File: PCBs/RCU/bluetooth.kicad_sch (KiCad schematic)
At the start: 33 parts

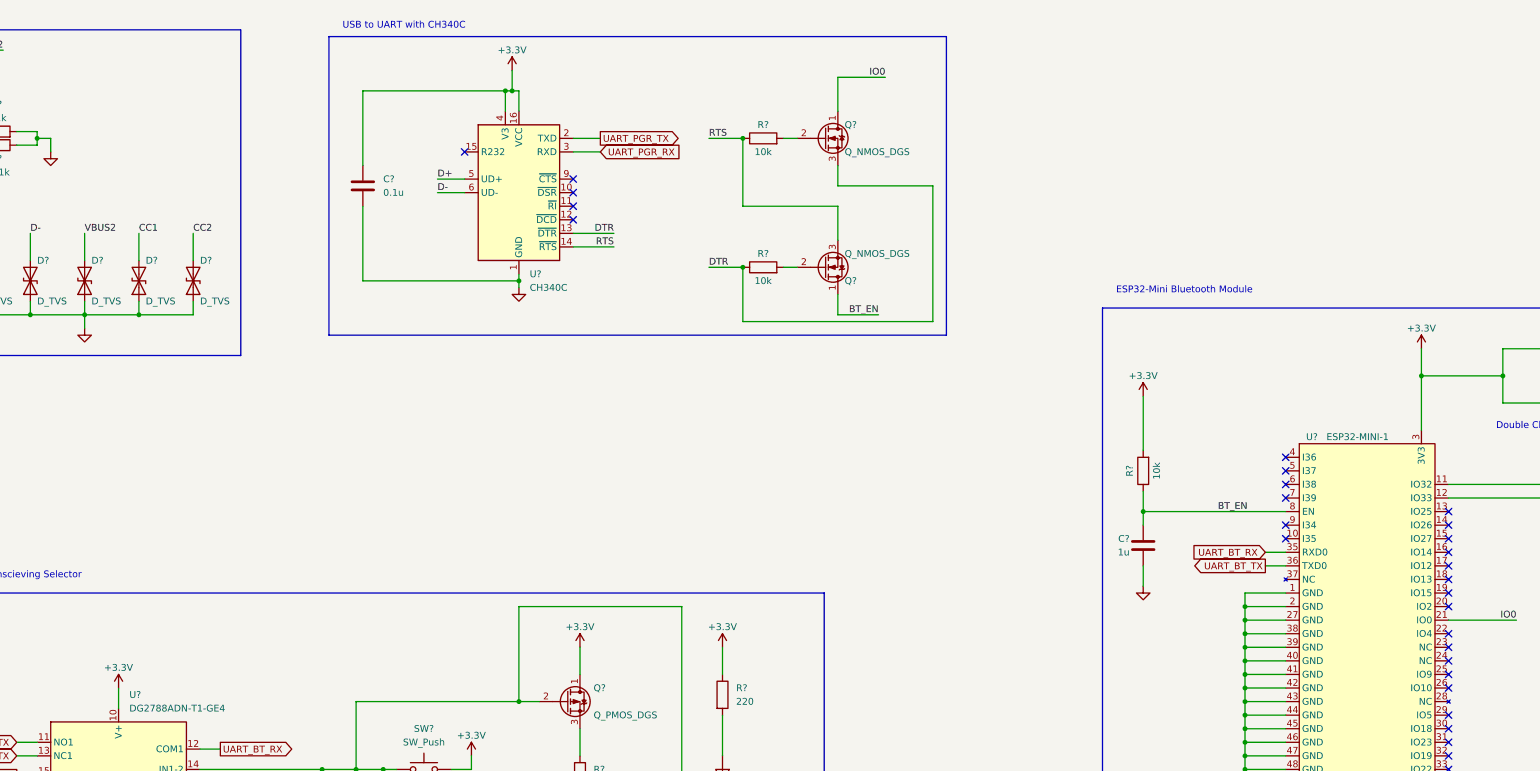
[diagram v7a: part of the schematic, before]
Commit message: Add battery filter circuit, corrected cap values for 3.3V regulators, used different output power floag for Bottom regulator so that it only powers the Bluetooth susbsystem
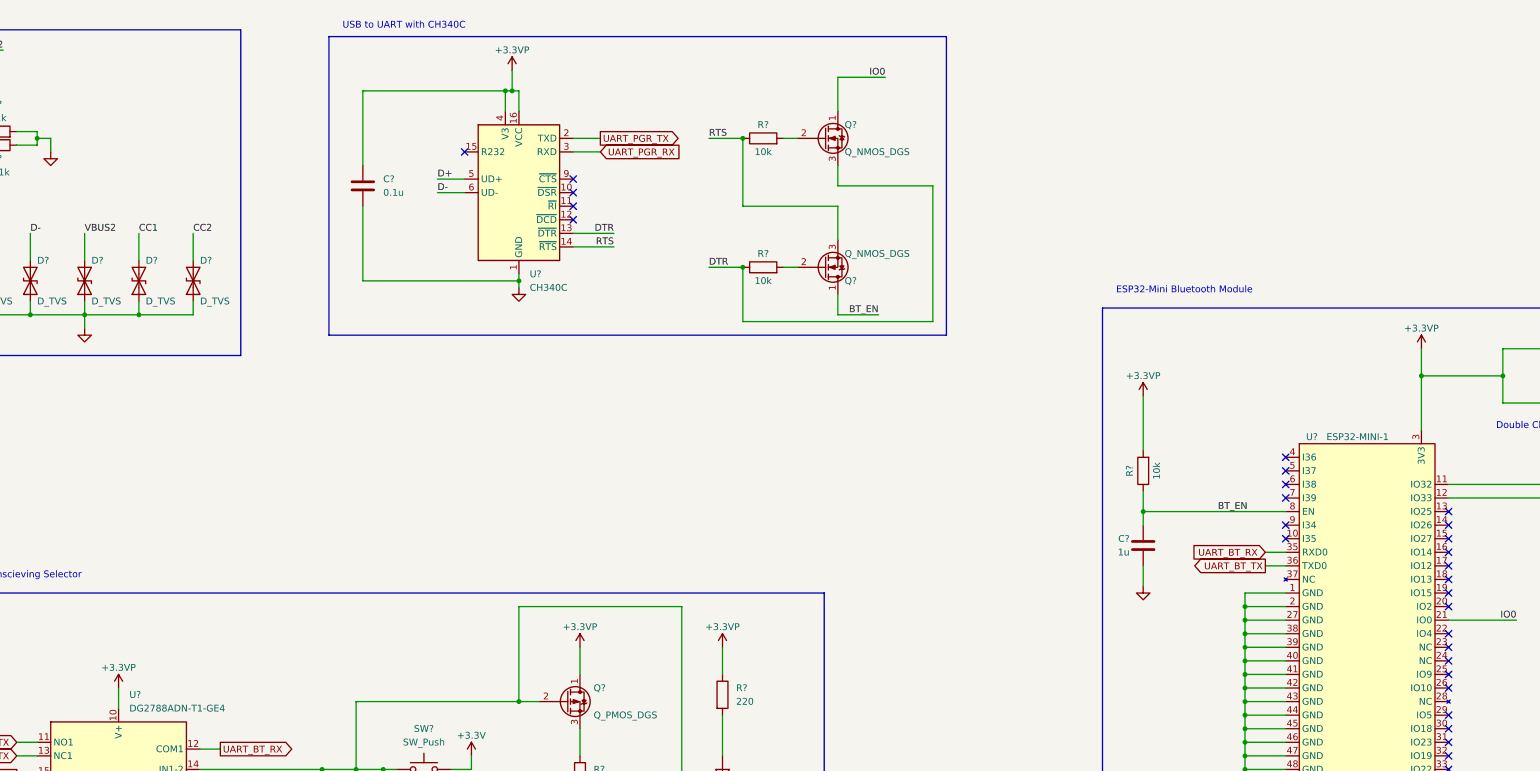
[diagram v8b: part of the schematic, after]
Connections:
- net +3V3: no longer C?.1, C?.1, C?.1, Q?.1 (D), R?.1, R?.2, U?.10 (V+), U?.16 (VCC), U?.3 (3V3), U?.4 (V3)
- new net +3.3VP: C?.1, C?.1, C?.1, Q?.1 (D), R?.1, R?.2, U?.10 (V+), U?.16 (VCC), U?.3 (3V3), U?.4 (V3)
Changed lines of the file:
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@@
     )
-  )
-  (symbol (lib_id "power:+3.3V") (at 340.36 91.44 0) (unit 1)
-    (in_bom yes) (on_board yes)
-    (property "Reference" "#PWR?" (id 0) (at 340.36 95.25 0)
-      (effects (font (size 1.27 1.27)) hide)
-    )
-    (property "Value" "+3.3V" (id 1) (at 340.36 87.63 0))
-    (property "Footprint" "" (id 2) (at 340.36 91.44 0)
-      (effects (font (size 1.27 1.27)) hide)
-    )
-    (property "Datasheet" "" (id 3) (at 340.36 91.44 0)
-      (effects (font (size 1.27 1.27)) hide)
-    )
-    (pin "1")
   )
   (symbol (lib_id "Device:C") (at 142.24 60.96 0) (unit 1)
@@
     (pin "1")
     (pin "2")
+  )
+  (symbol (lib_id "power:+3.3VP") (at 170.18 39.37 0) (unit 1)
+    (in_bom yes) (on_board yes)
+    (property "Reference" "#PWR?" (id 0) (at 173.99 40.64 0)
+      (effects (font (size 1.27 1.27)) hide)
+    )
+    (property "Value" "+3.3VP" (id 1) (at 170.18 35.56 0))
+    (property "Footprint" "" (id 2) (at 170.18 39.37 0)
+      (effects (font (size 1.27 1.27)) hide)
+    )
+    (property "Datasheet" "" (id 3) (at 170.18 39.37 0)
+      (effects (font (size 1.27 1.27)) hide)
+    )
+    (pin "1")
   )
   (symbol (lib_id "Device:Q_NMOS_DGS") (at 228.6 76.2 0) (mirror x) (unit 1)
@@
     )
     (property "Datasheet" "" (id 3) (at 288.29 135.89 0)
+      (effects (font (size 1.27 1.27)) hide)
+    )
+    (pin "1")
+  )
+  (symbol (lib_id "power:+3.3VP") (at 209.55 147.32 0) (unit 1)
+    (in_bom yes) (on_board yes)
+    (property "Reference" "#PWR?" (id 0) (at 213.36 148.59 0)
+      (effects (font (size 1.27 1.27)) hide)
+    )
+    (property "Value" "+3.3VP" (id 1) (at 209.55 143.51 0))
+    (property "Footprint" "" (id 2) (at 209.55 147.32 0)
+      (effects (font (size 1.27 1.27)) hide)
+    )
+    (property "Datasheet" "" (id 3) (at 209.55 147.32 0)
       (effects (font (size 1.27 1.27)) hide)
     )
@@
     (pin "2")
   )
-  (symbol (lib_id "power:+3.3V") (at 170.18 39.37 0) (unit 1)
-    (in_bom yes) (on_board yes)
-    (property "Reference" "#PWR?" (id 0) (at 170.18 43.18 0)
-      (effects (font (size 1.27 1.27)) hide)
-    )
-    (property "Value" "+3.3V" (id 1) (at 170.18 35.56 0))
-    (property "Footprint" "" (id 2) (at 170.18 39.37 0)
-      (effects (font (size 1.27 1.27)) hide)
-    )
-    (property "Datasheet" "" (id 3) (at 170.18 39.37 0)
+  (symbol (lib_id "power:+3.3VP") (at 340.36 91.44 0) (unit 1)
+    (in_bom yes) (on_board yes)
+    (property "Reference" "#PWR?" (id 0) (at 344.17 92.71 0)
+      (effects (font (size 1.27 1.27)) hide)
+    )
+    (property "Value" "+3.3VP" (id 1) (at 340.36 87.63 0))
+    (property "Footprint" "" (id 2) (at 340.36 91.44 0)
+      (effects (font (size 1.27 1.27)) hide)
+    )
+    (property "Datasheet" "" (id 3) (at 340.36 91.44 0)
+      (effects (font (size 1.27 1.27)) hide)
+    )
+    (pin "1")
+  )
+  (symbol (lib_id "power:+3.3VP") (at 182.88 147.32 0) (unit 1)
+    (in_bom yes) (on_board yes)
+    (property "Reference" "#PWR?" (id 0) (at 186.69 148.59 0)
+      (effects (font (size 1.27 1.27)) hide)
+    )
+    (property "Value" "+3.3VP" (id 1) (at 182.88 143.51 0))
+    (property "Footprint" "" (id 2) (at 182.88 147.32 0)
+      (effects (font (size 1.27 1.27)) hide)
+    )
+    (property "Datasheet" "" (id 3) (at 182.88 147.32 0)
       (effects (font (size 1.27 1.27)) hide)
     )
@@
     (pin "2")
   )
-  (symbol (lib_id "power:+3.3V") (at 182.88 147.32 0) (unit 1)
-    (in_bom yes) (on_board yes)
-    (property "Reference" "#PWR?" (id 0) (at 182.88 151.13 0)
-      (effects (font (size 1.27 1.27)) hide)
-    )
-    (property "Value" "+3.3V" (id 1) (at 182.88 143.51 0))
-    (property "Footprint" "" (id 2) (at 182.88 147.32 0)
-      (effects (font (size 1.27 1.27)) hide)
-    )
-    (property "Datasheet" "" (id 3) (at 182.88 147.32 0)
-      (effects (font (size 1.27 1.27)) hide)
-    )
-    (pin "1")
-  )
   (symbol (lib_id "Device:R") (at 209.55 156.21 0) (unit 1)
     (in_bom yes) (on_board yes) (fields_autoplaced)
@@
     (pin "1")
     (pin "2")
-  )
-  (symbol (lib_id "power:+3.3V") (at 96.52 154.94 0) (unit 1)
-    (in_bom yes) (on_board yes)
-    (property "Reference" "#PWR?" (id 0) (at 96.52 158.75 0)
-      (effects (font (size 1.27 1.27)) hide)
-    )
-    (property "Value" "+3.3V" (id 1) (at 96.52 151.13 0))
-    (property "Footprint" "" (id 2) (at 96.52 154.94 0)
-      (effects (font (size 1.27 1.27)) hide)
-    )
-    (property "Datasheet" "" (id 3) (at 96.52 154.94 0)
-      (effects (font (size 1.27 1.27)) hide)
-    )
-    (pin "1")
   )
   (symbol (lib_id "Device:R") (at 217.17 52.07 90) (unit 1)
@@
     (pin "2")
   )
-  (symbol (lib_id "power:+3.3V") (at 288.29 100.33 0) (unit 1)
-    (in_bom yes) (on_board yes)
-    (property "Reference" "#PWR?" (id 0) (at 288.29 104.14 0)
-      (effects (font (size 1.27 1.27)) hide)
-    )
-    (property "Value" "+3.3V" (id 1) (at 288.29 96.52 0))
+  (symbol (lib_id "Device:C") (at 369.57 101.6 90) (mirror x) (unit 1)
+    (in_bom yes) (on_board yes)
+    (property "Reference" "C?" (id 0) (at 368.3 100.33 90)
+      (effects (font (size 1.27 1.27)) (justify left))
+    )
+    (property "Value" "10u" (id 1) (at 374.65 100.33 90)
+      (effects (font (size 1.27 1.27)) (justify left))
+    )
+    (property "Footprint" "" (id 2) (at 373.38 102.5652 0)
+      (effects (font (size 1.27 1.27)) hide)
+    )
+    (property "Datasheet" "~" (id 3) (at 369.57 101.6 0)
+      (effects (font (size 1.27 1.27)) hide)
+    )
+    (pin "1")
+    (pin "2")
+  )
+  (symbol (lib_id "power:GND") (at 96.52 196.85 0) (unit 1)
+    (in_bom yes) (on_board yes) (fields_autoplaced)
+    (property "Reference" "#PWR?" (id 0) (at 96.52 203.2 0)
+      (effects (font (size 1.27 1.27)) hide)
+    )
+    (property "Value" "GND" (id 1) (at 96.52 201.93 0)
+      (effects (font (size 1.27 1.27)) hide)
+    )
+    (property "Footprint" "" (id 2) (at 96.52 196.85 0)
+      (effects (font (size 1.27 1.27)) hide)
+    )
+    (property "Datasheet" "" (id 3) (at 96.52 196.85 0)
+      (effects (font (size 1.27 1.27)) hide)
+    )
+    (pin "1")
+  )
+  (symbol (lib_id "power:+3.3VP") (at 288.29 100.33 0) (unit 1)
+    (in_bom yes) (on_board yes)
+    (property "Reference" "#PWR?" (id 0) (at 292.1 101.6 0)
+      (effects (font (size 1.27 1.27)) hide)
+    )
+    (property "Value" "+3.3VP" (id 1) (at 288.29 96.52 0))
     (property "Footprint" "" (id 2) (at 288.29 100.33 0)
       (effects (font (size 1.27 1.27)) hide)
@@
     (pin "1")
   )
-  (symbol (lib_id "power:+3.3V") (at 209.55 147.32 0) (unit 1)
-    (in_bom yes) (on_board yes)
-    (property "Reference" "#PWR?" (id 0) (at 209.55 151.13 0)
-      (effects (font (size 1.27 1.27)) hide)
-    )
-    (property "Value" "+3.3V" (id 1) (at 209.55 143.51 0))
-    (property "Footprint" "" (id 2) (at 209.55 147.32 0)
-      (effects (font (size 1.27 1.27)) hide)
-    )
-    (property "Datasheet" "" (id 3) (at 209.55 147.32 0)
-      (effects (font (size 1.27 1.27)) hide)
-    )
-    (pin "1")
-  )
-  (symbol (lib_id "Device:C") (at 369.57 101.6 90) (mirror x) (unit 1)
-    (in_bom yes) (on_board yes)
-    (property "Reference" "C?" (id 0) (at 368.3 100.33 90)
-      (effects (font (size 1.27 1.27)) (justify left))
-    )
-    (property "Value" "10u" (id 1) (at 374.65 100.33 90)
-      (effects (font (size 1.27 1.27)) (justify left))
-    )
-    (property "Footprint" "" (id 2) (at 373.38 102.5652 0)
-      (effects (font (size 1.27 1.27)) hide)
-    )
-    (property "Datasheet" "~" (id 3) (at 369.57 101.6 0)
-      (effects (font (size 1.27 1.27)) hide)
-    )
-    (pin "1")
-    (pin "2")
-  )
-  (symbol (lib_id "power:GND") (at 96.52 196.85 0) (unit 1)
-    (in_bom yes) (on_board yes) (fields_autoplaced)
-    (property "Reference" "#PWR?" (id 0) (at 96.52 203.2 0)
-      (effects (font (size 1.27 1.27)) hide)
-    )
-    (property "Value" "GND" (id 1) (at 96.52 201.93 0)
-      (effects (font (size 1.27 1.27)) hide)
-    )
-    (property "Footprint" "" (id 2) (at 96.52 196.85 0)
-      (effects (font (size 1.27 1.27)) hide)
-    )
-    (property "Datasheet" "" (id 3) (at 96.52 196.85 0)
-      (effects (font (size 1.27 1.27)) hide)
-    )
-    (pin "1")
-  )
   (symbol (lib_id "Device:Q_NMOS_DGS") (at 228.6 52.07 0) (unit 1)
     (in_bom yes) (on_board yes)
@@
     (pin "2")
   )
+  (symbol (lib_id "power:+3.3VP") (at 96.52 154.94 0) (unit 1)
+    (in_bom yes) (on_board yes)
+    (property "Reference" "#PWR?" (id 0) (at 100.33 156.21 0)
+      (effects (font (size 1.27 1.27)) hide)
+    )
+    (property "Value" "+3.3VP" (id 1) (at 96.52 151.13 0))
+    (property "Footprint" "" (id 2) (at 96.52 154.94 0)
+      (effects (font (size 1.27 1.27)) hide)
+    )
+    (property "Datasheet" "" (id 3) (at 96.52 154.94 0)
+      (effects (font (size 1.27 1.27)) hide)
+    )
+    (pin "1")
+  )
   (symbol (lib_id "Device:Q_NMOS_DGS") (at 207.01 185.42 0) (unit 1)
